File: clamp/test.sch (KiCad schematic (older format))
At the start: 1 part

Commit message: update
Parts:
- removed R14: R, Resistors_SMD:R_1206, symbol R
- added P?: CONN_01X10, symbol CONN_01X10
- added R?: R, symbol R
- added R? (x2): R, Resistors_SMD:R_1206, symbol R
- added U?: DG444, symbol DG444
- added U?: LM741, symbol LM741
- added U?: LM741, Housings_SOIC:SOIC-8_3.9x4.9mm_Pitch1.27mm, symbol LM741
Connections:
- net labels added: 3.3V, GND, IN, IN_CTL, REF, REF_NEG_CTL, REF_PLUS_CTL, RESET
- wire segments 2 -> 40
- no-connect marks 0 -> 2
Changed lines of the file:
@@
 Comment4 ""
 $EndDescr
-Text GLabel 4750 1850 0    60   Input ~ 0
-+VE
-Wire Wire Line
-	4750 1850 5100 1850
-$Comp
-L R R14
-U 1 1 580BAAC7
-P 5250 1850
-F 0 "R14" V 5330 1850 50  0000 C CNN
-F 1 "R" V 5250 1850 50  0000 C CNN
-F 2 "Resistors_SMD:R_1206" V 5180 1850 50  0001 C CNN
-F 3 "" H 5250 1850 50  0000 C CNN
-	1    5250 1850
+Text GLabel 4500 2800 2    60   Input ~ 0
++VE
+Text GLabel 2450 2800 0    60   Input ~ 0
+-VE
+$Comp
+L DG444 U?
+U 1 1 585BA0F9
+P 3500 3000
+AR Path="/580BA788/585BA0F9" Ref="U?"  Part="1"
+AR Path="/585BBA35/585BA0F9" Ref="U?"  Part="1"
+F 0 "U?" H 3650 3700 50  0000 L CNN
+F 1 "DG444" H 3550 2600 50  0000 L CNN
+F 2 "" H 3500 3000 50  0000 C CNN
+F 3 "" H 3500 3000 50  0000 C CNN
+	1    3500 3000
+	1    0    0    -1
+$EndComp
+Wire Wire Line
+	4100 2800 4500 2800
+Wire Wire Line
+	2450 2800 2900 2800
+Text GLabel 2450 2900 0    60   Input ~ 0
+GND
+Wire Wire Line
+	2450 2900 2900 2900
+$Comp
+L CONN_01X10 P?
+U 1 1 585BA5AA
+P 1300 1250
+AR Path="/580BA788/585BA5AA" Ref="P?"  Part="1"
+AR Path="/585BBA35/585BA5AA" Ref="P?"  Part="1"
+F 0 "P?" H 1300 1800 50  0000 C CNN
+F 1 "CONN_01X10" V 1400 1250 50  0000 C CNN
+F 2 "" H 1300 1250 50  0000 C CNN
+F 3 "" H 1300 1250 50  0000 C CNN
+	1    1300 1250
+	-1   0    0    1
+$EndComp
+Text GLabel 1750 800  2    60   Input ~ 0
++VE
+Text GLabel 1750 900  2    60   Input ~ 0
+GND
+Text GLabel 1750 1000 2    60   Input ~ 0
+-VE
+Wire Wire Line
+	1500 800  1750 800
+Wire Wire Line
+	1500 900  1750 900
+Wire Wire Line
+	1500 1000 1750 1000
+Wire Wire Line
+	4100 2600 4200 2600
+Wire Wire Line
+	4200 2600 4200 2100
+Wire Wire Line
+	2750 2600 2900 2600
+Connection ~ 4200 2100
+Text GLabel 1200 2700 0    60   Input ~ 0
+REF
+Wire Wire Line
+	1200 2700 2900 2700
+Text GLabel 4500 3200 2    60   Input ~ 0
+RESET
+Wire Wire Line
+	4100 3200 4500 3200
+Text GLabel 4500 2900 2    60   Input ~ 0
+3.3V
+Wire Wire Line
+	4500 2900 4100 2900
+Wire Wire Line
+	4100 3000 5600 3000
+Wire Wire Line
+	4100 3100 5750 3100
+$Comp
+L LM741 U?
+U 1 1 585BA828
+P 6200 2000
+AR Path="/580BA788/585BA828" Ref="U?"  Part="1"
+AR Path="/585BBA35/585BA828" Ref="U?"  Part="1"
+F 0 "U?" H 6200 2250 50  0000 L CNN
+F 1 "LM741" H 6200 2150 50  0000 L CNN
+F 2 "" H 6250 2050 50  0000 C CNN
+F 3 "" H 6350 2150 50  0000 C CNN
+	1    6200 2000
+	1    0    0    -1
+$EndComp
+$Comp
+L R R?
+U 1 1 585BA8B1
+P 5200 2100
+AR Path="/580BA788/585BA8B1" Ref="R?"  Part="1"
+AR Path="/585BBA35/585BA8B1" Ref="R?"  Part="1"
+F 0 "R?" V 5280 2100 50  0000 C CNN
+F 1 "R" V 5200 2100 50  0000 C CNN
+F 2 "" V 5130 2100 50  0000 C CNN
+F 3 "" H 5200 2100 50  0000 C CNN
+	1    5200 2100
 	0    1    1    0
 $EndComp
 Wire Wire Line
-	5400 1850 5750 1850
-Text GLabel 5750 1850 2    60   Input ~ 0
--VE
+	2750 2100 5050 2100
+Wire Wire Line
+	5350 2100 5900 2100
+Text GLabel 5300 1900 0    60   Input ~ 0
+GND
+Wire Wire Line
+	5600 3000 5600 2100
+Connection ~ 5600 2100
+Text GLabel 2450 3200 0    60   Input ~ 0
+IN_CTL
+Wire Wire Line
+	2900 3200 2450 3200
+Wire Wire Line
+	2750 3100 2900 3100
+Wire Wire Line
+	5300 1900 5900 1900
+Wire Wire Line
+	5750 3100 5750 1900
+Connection ~ 5750 1900
+Text GLabel 6100 1500 1    60   Input ~ 0
++VE
+Wire Wire Line
+	6100 1500 6100 1700
+Text GLabel 6100 2500 3    60   Input ~ 0
+-VE
+Wire Wire Line
+	6650 2150 6100 2150
+Wire Wire Line
+	6100 2300 6100 2500
+Wire Wire Line
+	2950 4200 4200 4200
+$Comp
+L LM741 U?
+U 1 1 585BE628
+P 2650 4200
+F 0 "U?" H 2650 4450 50  0000 L CNN
+F 1 "LM741" H 2650 4350 50  0000 L CNN
+F 2 "Housings_SOIC:SOIC-8_3.9x4.9mm_Pitch1.27mm" H 2700 4250 50  0001 C CNN
+F 3 "" H 2800 4350 50  0000 C CNN
+	1    2650 4200
+	1    0    0    -1
+$EndComp
+Wire Wire Line
+	2100 4100 2350 4100
+Wire Wire Line
+	3050 4200 3050 4850
+Wire Wire Line
+	3050 4850 2750 4850
+$Comp
+L R R?
+U 1 1 585BE632
+P 2650 4850
+F 0 "R?" V 2730 4850 50  0000 C CNN
+F 1 "R" V 2650 4850 50  0000 C CNN
+F 2 "Resistors_SMD:R_1206" V 2580 4850 50  0001 C CNN
+F 3 "" H 2650 4850 50  0000 C CNN
+	1    2650 4850
+	0    1    1    0
+$EndComp
+$Comp
+L R R?
+U 1 1 585BE639
+P 1900 4300
+F 0 "R?" V 1980 4300 50  0000 C CNN
+F 1 "R" V 1900 4300 50  0000 C CNN
+F 2 "Resistors_SMD:R_1206" V 1830 4300 50  0001 C CNN
+F 3 "" H 1900 4300 50  0000 C CNN
+	1    1900 4300
+	0    1    1    0
+$EndComp
+Wire Wire Line
+	2050 4300 2350 4300
+Wire Wire Line
+	2250 4300 2250 4850
+Wire Wire Line
+	2250 4850 2500 4850
+Connection ~ 2250 4300
+Text GLabel 2550 3900 1    60   Input ~ 0
++VE
+Text GLabel 2550 4500 3    60   Input ~ 0
+-VE
+NoConn ~ 2650 4500
+NoConn ~ 2750 4500
+Connection ~ 3050 4200
+Text GLabel 2100 3900 1    60   Input ~ 0
+GND
+Wire Wire Line
+	2100 3900 2100 4100
+Wire Wire Line
+	4100 2700 4200 2700
+Wire Wire Line
+	4200 2700 4200 4200
+Wire Wire Line
+	1500 2700 1500 4300
+Connection ~ 1500 2700
+Wire Wire Line
+	2750 2100 2750 3100
+Connection ~ 2750 2600
+Text GLabel 2450 2500 0    60   Input ~ 0
+REF_PLUS_CTL
+Wire Wire Line
+	2900 2500 2450 2500
+Text GLabel 4500 2500 2    60   Input ~ 0
+REF_NEG_CTL
+Wire Wire Line
+	4500 2500 4100 2500
+Wire Wire Line
+	2900 3000 1200 3000
+Text GLabel 1200 3000 0    60   Input ~ 0
+IN
+Wire Wire Line
+	1500 4300 1750 4300
 $EndSCHEMATC

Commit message: update
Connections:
- wire segments 40 -> 46
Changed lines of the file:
@@
 REF
 Wire Wire Line
-	1200 2700 2900 2700
+	1200 2700 1500 2700
+Wire Wire Line
+	1500 2700 2900 2700
 Text GLabel 4500 3200 2    60   Input ~ 0
 RESET
@@
 $EndComp
 Wire Wire Line
-	2750 2100 5050 2100
+	2750 2100 4200 2100
 Wire Wire Line
-	5350 2100 5900 2100
+	4200 2100 5050 2100
+Wire Wire Line
+	5350 2100 5600 2100
+Wire Wire Line
+	5600 2100 5900 2100
 Text GLabel 5300 1900 0    60   Input ~ 0
 GND
@@
 	2750 3100 2900 3100
 Wire Wire Line
-	5300 1900 5900 1900
+	5300 1900 5750 1900
+Wire Wire Line
+	5750 1900 5900 1900
 Wire Wire Line
 	5750 3100 5750 1900
@@
 -VE
 Wire Wire Line
-	6650 2150 6100 2150
-Wire Wire Line
 	6100 2300 6100 2500
 Wire Wire Line
-	2950 4200 4200 4200
+	2950 4200 3050 4200
+Wire Wire Line
+	3050 4200 4200 4200
 $Comp
 L LM741 U?
@@
 $EndComp
 Wire Wire Line
-	2050 4300 2350 4300
+	2050 4300 2250 4300
+Wire Wire Line
+	2250 4300 2350 4300
 Wire Wire Line
 	2250 4300 2250 4850
@@
 Connection ~ 1500 2700
 Wire Wire Line
-	2750 2100 2750 3100
+	2750 2100 2750 2600
+Wire Wire Line
+	2750 2600 2750 3100
 Connection ~ 2750 2600
 Text GLabel 2450 2500 0    60   Input ~ 0

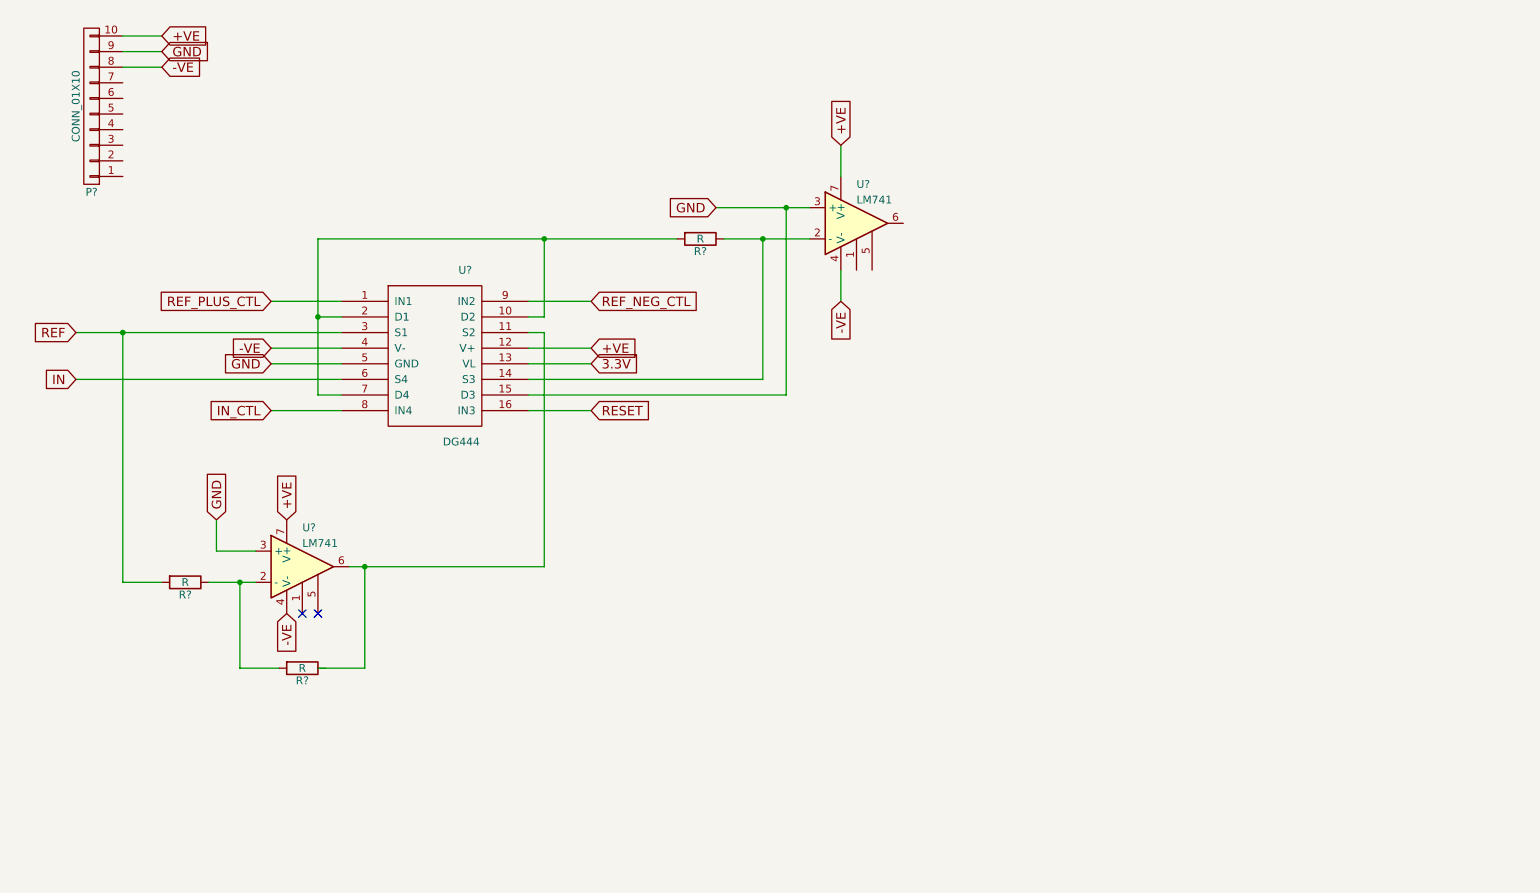
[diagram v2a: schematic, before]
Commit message: add ADC
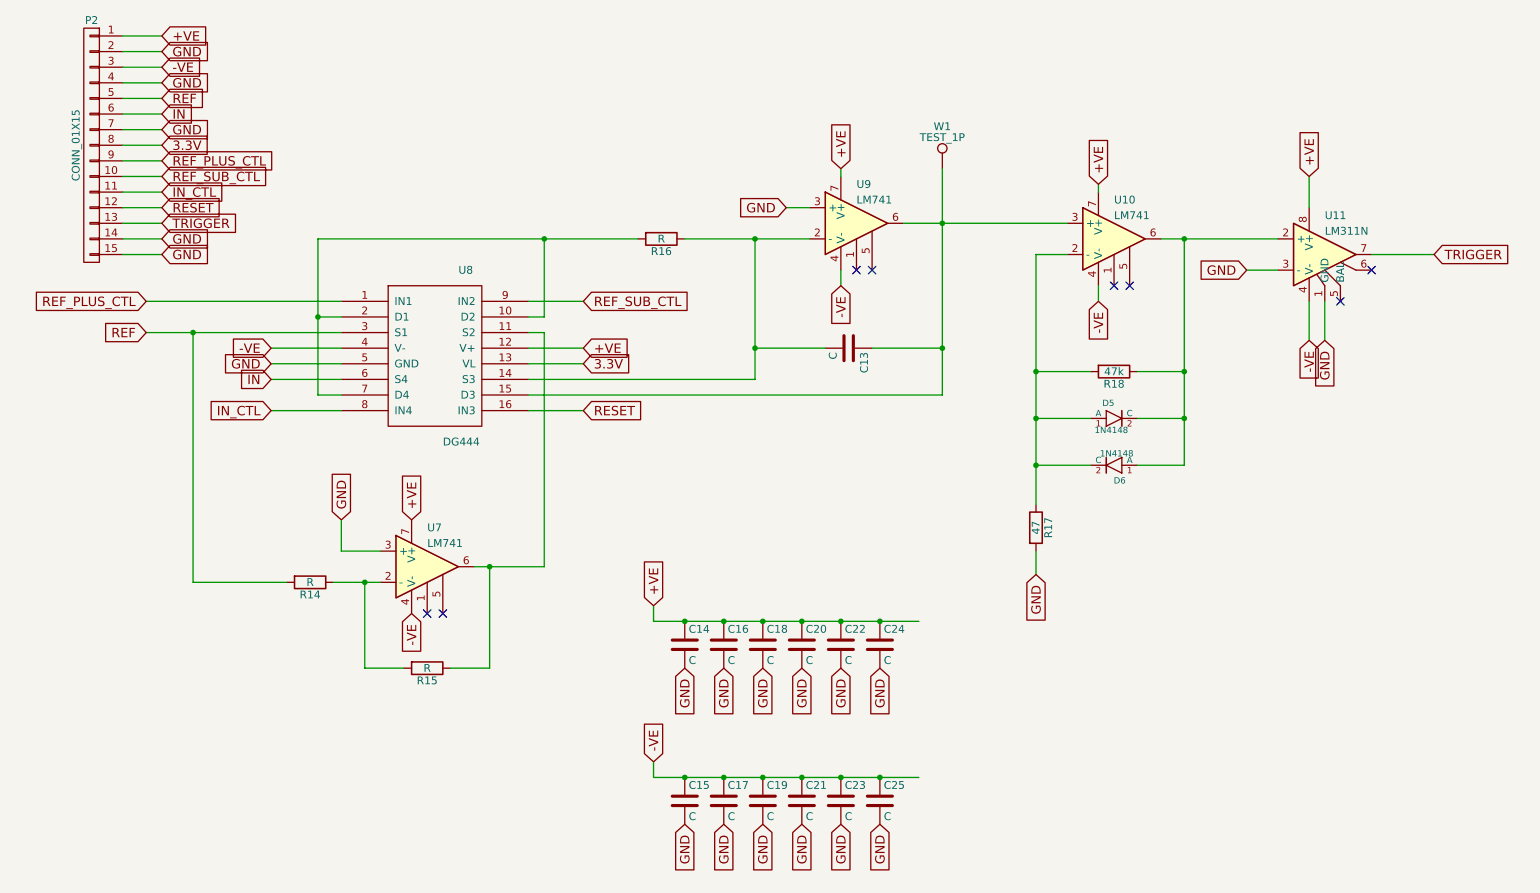
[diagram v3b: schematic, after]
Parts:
- removed P?: CONN_01X10, symbol CONN_01X10
- added C13: C, symbol C
- added C14, C15, C16, C17, C18, C19, C20, C21, C22, C23, C24, C25: C, Capacitors_SMD:C_1206, symbol C
- added D5, D6: 1N4148, DO35, symbol 1N4148
- added P2: CONN_01X15, symbol CONN_01X15
- added R17: 47, symbol R
- added R18: 47k, symbol R
- added U10: LM741, symbol LM741
- added U11: LM311N, symbol LM311N
- added W1: TEST_1P, symbol TEST_1P
- gave numbers to parts that had none: 6
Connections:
- net +VE: now also C14.1, C16.1, C18.1, C20.1, C22.1, C24.1, P2.1 (P1), U10.7 (V+), U11.8 (V+)
- net -VE: now also C15.1, C17.1, C19.1, C21.1, C23.1, C25.1, P2.3 (P3), U10.4 (V-), U11.4 (V-)
- net 3.3V: now also P2.8 (P8)
- net GND: now also C14.2, C15.2, C16.2, C17.2, C18.2, C19.2, C20.2, C21.2, C22.2, C23.2, C24.2, C25.2, P2.14 (P14), P2.15 (P15), P2.2 (P2), P2.4 (P4), P2.7 (P7), R17.2, U11.1 (GND), U11.3 (-); no longer U8.15 (D3)
- net IN: now also P2.6 (P6)
- net IN_CTL: now also P2.11 (P11)
- net REF: now also P2.5 (P5)
- net REF_PLUS_CTL: now also P2.9 (P9)
- net RESET: now also P2.12 (P12)
- net at U7.6, U8.11 (S2): now also R15.1
- net at R16.1, U8.14 (S3), U9.2 (-): now also C13.2
- net at U9.6: now also U8.15 (D3), C13.1, U10.3 (+), W1.1
- net REF_NEG_CTL renamed REF_SUB_CTL
- net REF_SUB_CTL: now also P2.10 (P10)
- new net: D5.1 (A), D6.2 (C), R17.1, R18.2, U10.2 (-)
- new net: D5.2 (C), D6.1 (A), R18.1, U10.6, U11.2 (+)
- new net TRIGGER: P2.13 (P13), U11.7
- no-connect marks 2 -> 8
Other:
- moved on the sheet: R14, R15, R16, U7
